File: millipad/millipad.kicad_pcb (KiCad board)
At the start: 2 copper layers, 131.8 x 63.5 mm, 51 parts, among them SW1 SW_Push, SW2 Rotary_Encoder_Switch, U1 ATmega32U4-AU, U2 PRTR5V0U2X, Y1 16MHz

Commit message: 3d work
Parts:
- added G***: LOGO, jirou-design:jirou-design-pcb-logo-inverse, F.Cu at (111.1, 52.4)

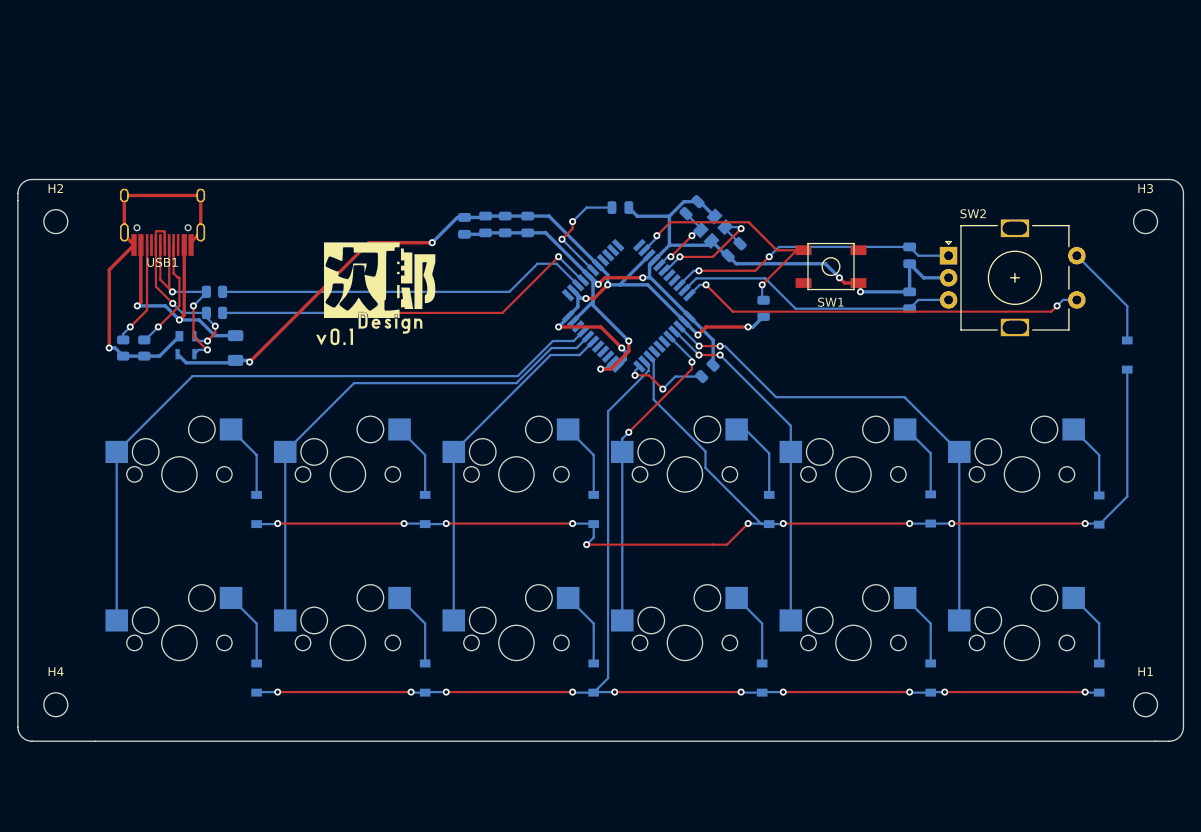
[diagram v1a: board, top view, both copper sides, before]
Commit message: Rewired CPU to fit OLED
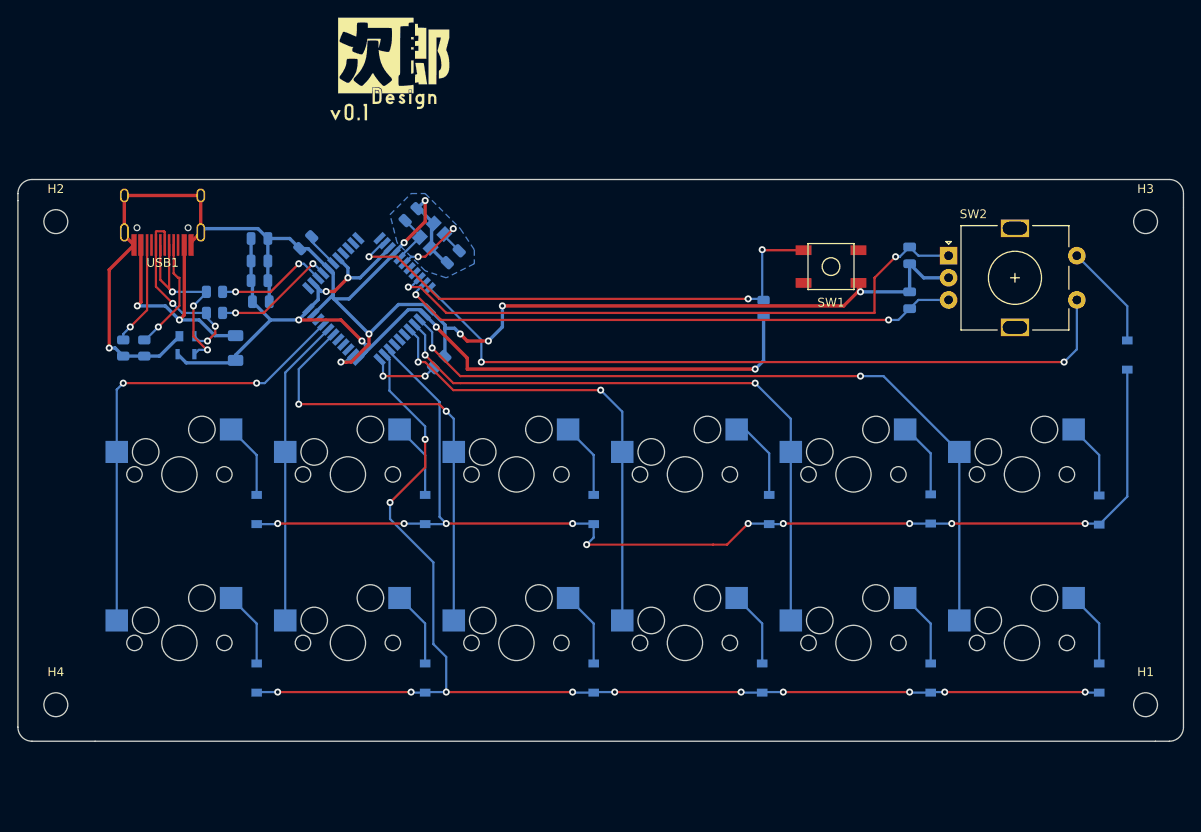
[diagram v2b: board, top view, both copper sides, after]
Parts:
- moved C7 35.8 mm to (103.2, 46.8), turned to 225 degrees
- moved C5 31.8 mm to (115.1, 43.7)
- moved Y1 31.8 mm to (117.5, 46.0)
- moved C4 31.8 mm to (119.9, 48.4)
- moved C6 30.4 mm to (98.0, 46.4), turned to 0 degrees
- moved R4 30.3 mm to (118.3, 60.3)
- moved U1 29.4 mm to (110.3, 53.2)
- moved C3 28.1 mm to (98.0, 48.9), turned to 0 degrees
- moved C2 26.3 mm to (98.0, 51.1), turned to 0 degrees
- moved G*** 25.4 mm to (112.7, 27.0)
- moved C1 24.6 mm to (98.1, 53.5), turned to 0 degrees
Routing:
- net COL6: track 46.1 -> 84.3 mm
- net ENC_A: track 32.6 -> 69.8 mm
- net GND: track 157.0 -> 193.4 mm, vias 7 -> 9
- net ENC_B: track 32.2 -> 64.1 mm, vias 0 -> 2
- net COL4: track 39.6 -> 71.1 mm
- net COL5: track 56.6 -> 87.3 mm
- net Net-(R3-Pad2): track 28.9 -> 59.3 mm, vias 2 -> 3
- net Net-(R2-Pad1): track 44.5 -> 14.1 mm
- net Net-(R1-Pad1): track 42.5 -> 12.8 mm, vias 0 -> 2
- net COL0: track 77.4 -> 52.5 mm, vias 0 -> 2
- net COL1: track 58.7 -> 34.9 mm
- net COL3: track 36.4 -> 53.1 mm
- net COL2: track 40.0 -> 50.5 mm, vias 0 -> 2
- net Net-(C7-Pad1): track 12.6 -> 4.00 mm, vias 2 -> 0
- net +5V: track 106.5 -> 113.4 mm, vias 8 -> 6
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- added copper zone on B.Cu, net GND

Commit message: Added SSD1306 128x64 OLED Breakout Board
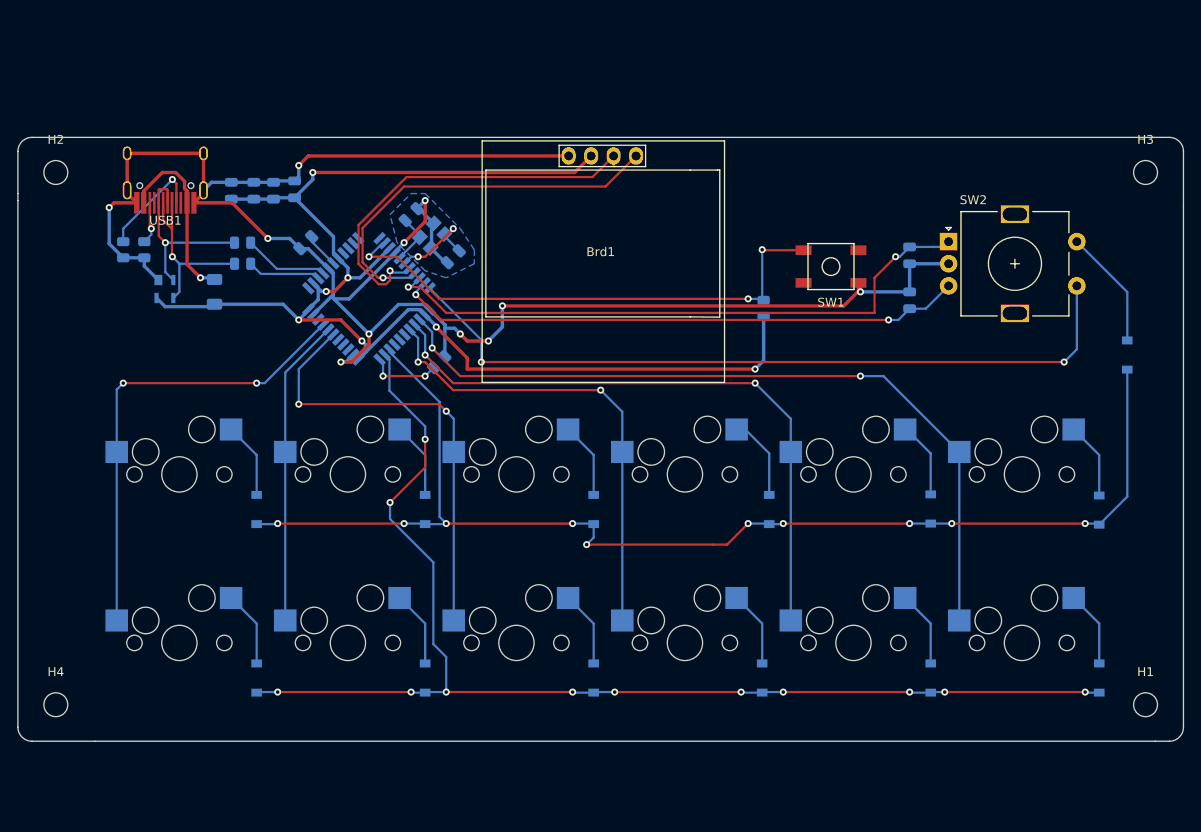
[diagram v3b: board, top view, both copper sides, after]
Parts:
- removed G***: LOGO, jirou-design:jirou-design-pcb-logo-inverse
- added Brd1: SSD1306, SSD1306:128x64OLED, F.Cu at (136.5, 47.6)
- U2: value PRTR5V0U2X -> SOT143B_NXP
- moved C1 13.3 mm to (101.9, 40.8), turned to 90 degrees
- moved R5 11.4 mm to (84.9, 47.6)
- moved R6 11.4 mm to (82.5, 47.6)
- moved C2 10.3 mm to (99.5, 41.0), turned to 90 degrees
- moved R2 8.55 mm to (96.0, 46.8)
- moved C3 7.97 mm to (97.3, 41.0), turned to 90 degrees
- moved U2 6.78 mm to (87.3, 52.1)
- moved F1 6.78 mm to (92.9, 52.4)
- moved C6 6.27 mm to (94.8, 41.0), turned to 90 degrees
- moved H2 5.56 mm to (74.9, 38.9)
- moved H3 5.56 mm to (198.1, 38.9)
- moved USB1 4.77 mm to (87.3, 34.1)
- moved R1 4.49 mm to (96.0, 49.2)
- moved SW2 1.59 mm to (183.4, 49.2)
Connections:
- U1 pad 18: Net-(U1-Pad18) -> SCL
- U1 pad 19: Net-(U1-Pad19) -> SDA
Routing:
- net SCL: track 0.00 -> 45.9 mm, vias 0 -> 1
- net SDA: track 0.00 -> 45.0 mm, vias 0 -> 1
- net +5V: track 113.4 -> 156.2 mm, vias 6 -> 7
- net GND: track 193.4 -> 223.8 mm, vias 9 -> 11
- net VCC: track 28.3 -> 20.5 mm, vias 2 -> 1
- net Net-(R5-Pad1): track 11.9 -> 4.78 mm
- net Net-(R2-Pad1): track 14.1 -> 9.64 mm, vias 2 -> 0
- net Net-(R1-Pad1): track 12.8 -> 8.32 mm, vias 2 -> 0
- net D-: track 24.7 -> 21.0 mm, vias 3 -> 1
- net COL6: track 84.3 -> 85.9 mm
- net Net-(D13-Pad2): track 11.9 -> 13.5 mm
- net ENC_B: track 64.1 -> 64.7 mm
- net Net-(R6-Pad1): track 12.8 -> 12.2 mm
- net D+: track 21.0 -> 21.2 mm, vias 3 -> 1
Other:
- board size 131.8 x 63.5 mm -> 131.8 x 68.3 mm

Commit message: Added pushbutton and isp flash headers
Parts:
- added D14: D_Small, Diode_SMD:D_SOD-123, B.Cu at (124.6, 106.4)
- added D15: D_Small, Diode_SMD:D_SOD-123, B.Cu at (148.4, 106.4)
- added J1: 6P6C, Connector_PinSocket_1.00mm:PinSocket_2x03_P1.00mm_Vertical_SMD, F.Cu at (75.4, 60.3)
- added SW3: SW_Push, random-keyboard-parts:SKQG-1155865, F.Cu at (131.8, 106.4)
- added SW4: SW_Push, random-keyboard-parts:SKQG-1155865, F.Cu at (141.3, 106.4)
- U2: value SOT143B_NXP -> PRTR5V0U2X
- moved H1 8.10 mm to (198.1, 107.2)
- moved H4 8.10 mm to (74.9, 107.2)
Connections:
- net +5V renamed KEYBOARD_VCC
- net GND renamed KEYBOARD_GND
- net Net-(R3-Pad2) renamed KEYBOARD_RESET
- U1 pad 10: Net-(U1-Pad10) -> B2_MOSI
- U1 pad 11: Net-(U1-Pad11) -> B3_MISO
- U1 pad 37: Net-(U1-Pad37) -> ROW2
- U1 pad 9: Net-(U1-Pad9) -> B1_SCLK
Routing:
- net KEYBOARD_RESET: track 59.3 -> 148.2 mm, vias 3 -> 6
- net ROW2: track 0.00 -> 83.9 mm
- net B2_MOSI: track 0.00 -> 46.9 mm, vias 0 -> 3
- net B3_MISO: track 0.00 -> 40.9 mm, vias 0 -> 1
- net B1_SCLK: track 0.00 -> 39.1 mm, vias 0 -> 1
- net COL2: track 50.5 -> 69.1 mm, vias 2 -> 3
- net COL3: track 53.1 -> 68.4 mm, vias 2 -> 3
- net KEYBOARD_VCC: track 156.2 -> 171.2 mm, vias 7 -> 8
- net KEYBOARD_GND: track 223.8 -> 236.9 mm, vias 11 -> 12
- net Net-(D14-Pad2): track 0.00 -> 11.4 mm, vias 0 -> 1
- net Net-(D15-Pad2): track 0.00 -> 4.18 mm, vias 0 -> 1
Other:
- board size 131.8 x 68.3 mm -> 131.8 x 76.2 mm

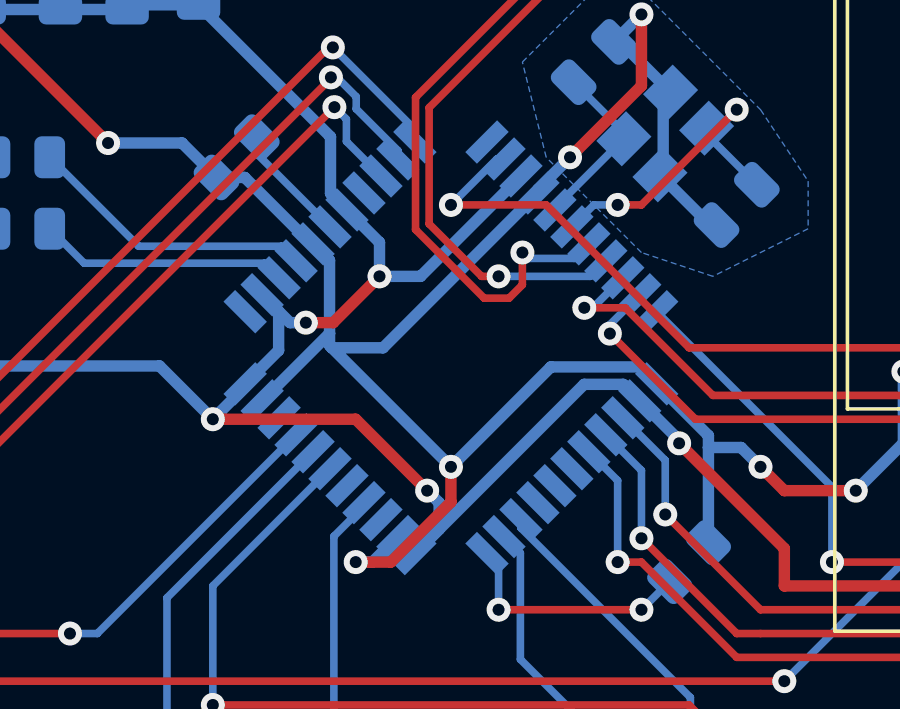
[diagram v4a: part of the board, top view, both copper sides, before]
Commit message: Generated BOM, POS, STEP for Plate Assembly
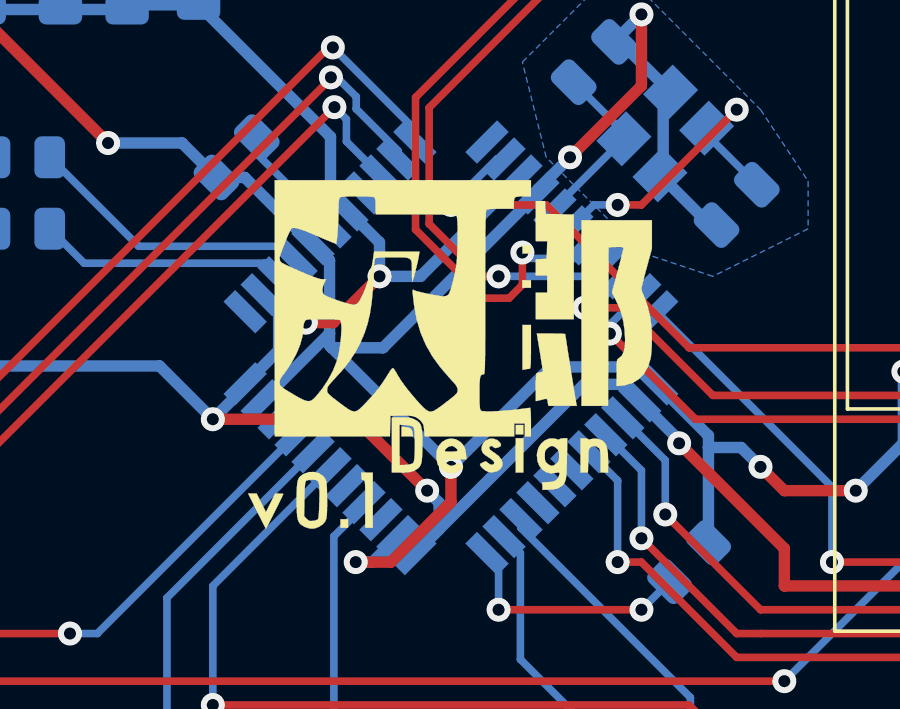
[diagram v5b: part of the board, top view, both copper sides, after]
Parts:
- added G***: LOGO, jirou-design:jirou-design-pcb-logo-inverse, F.Cu at (110.3, 53.2)
